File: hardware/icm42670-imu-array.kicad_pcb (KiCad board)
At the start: 4 copper layers, 40 x 40 mm, 63 parts, among them J1 TC2030-NL, J2 USB_B_Micro, J3 Conn_02x10_Odd_Even, SW1 PTS810, U1 ICM-42670-P, U10 MCP73812T-420I-OT, U2 ICM-42670-P, U3 ICM-42670-P, U4 ICM-42670-P, U5 ICM-42670-P, U6 ICM-42670-P, U7 ICM-42670-P, U8 ICM-42670-P, U9 MDBT50Q-P1MV2

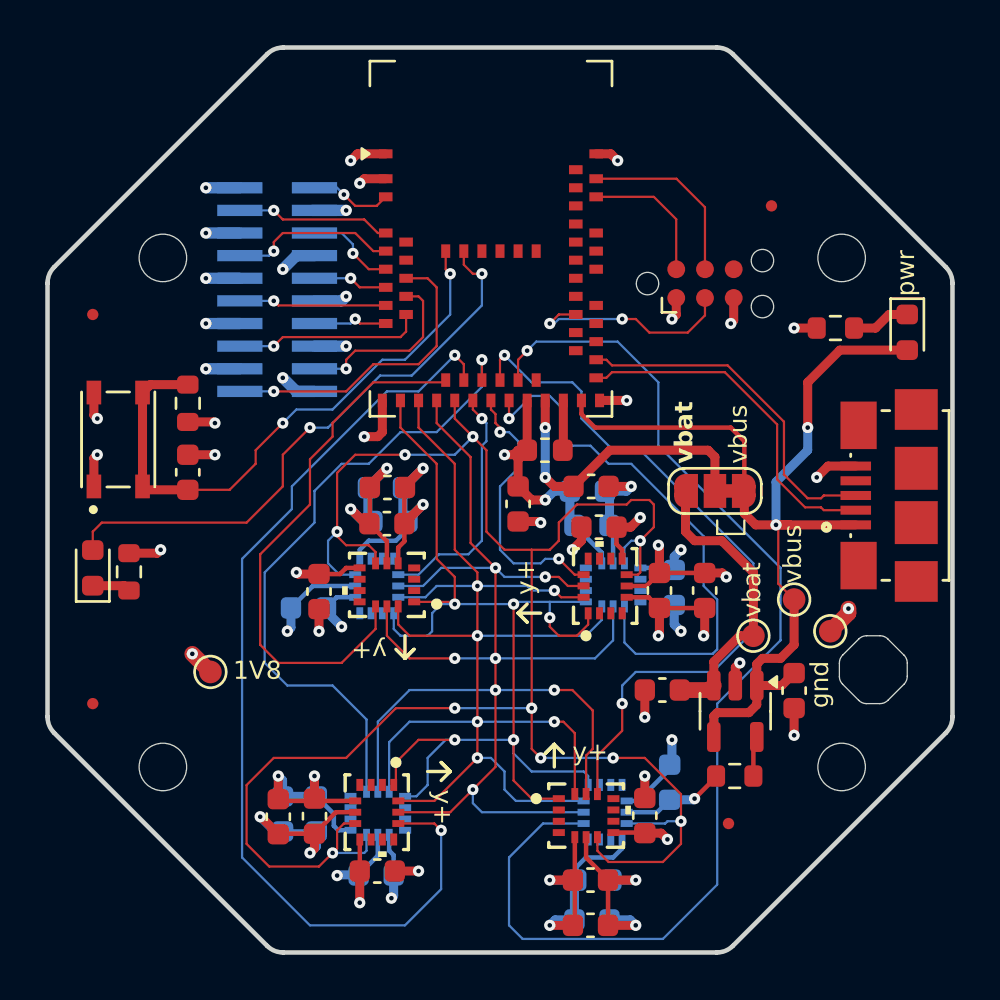
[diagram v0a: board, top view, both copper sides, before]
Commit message: feat: add round tracks
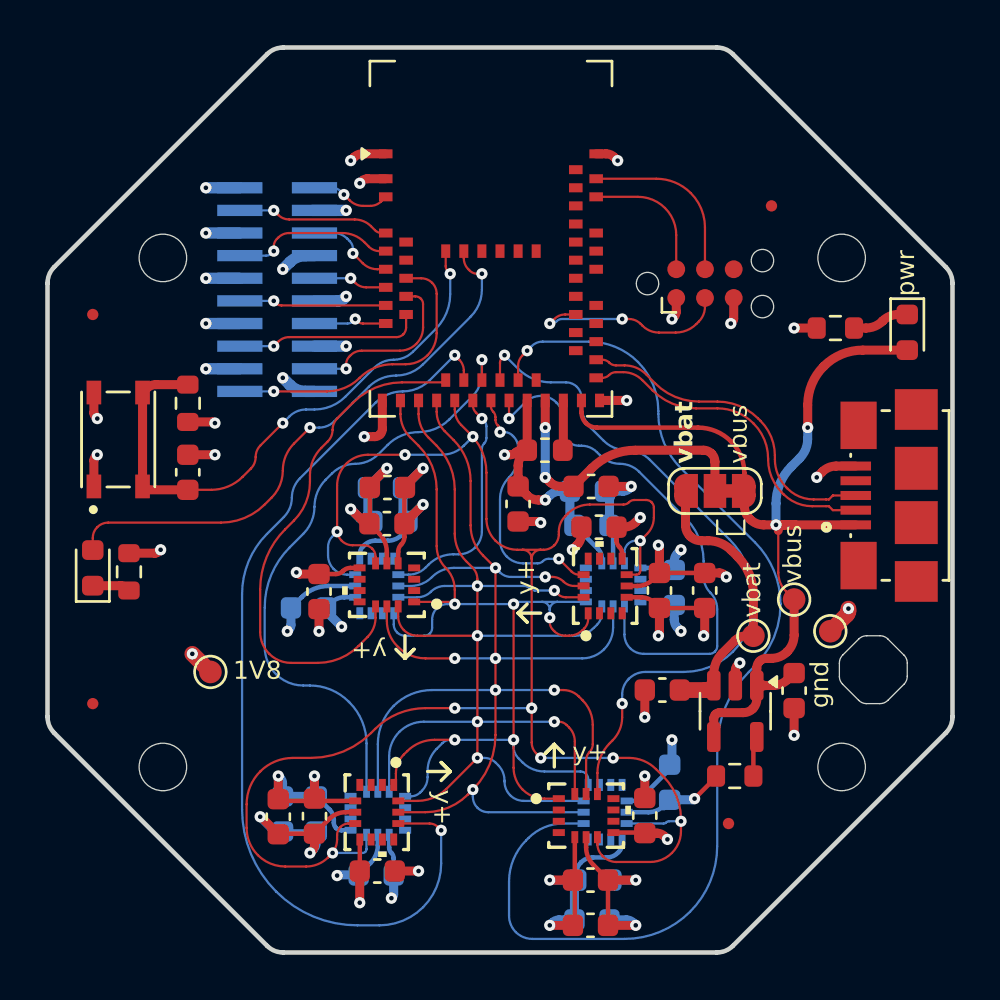
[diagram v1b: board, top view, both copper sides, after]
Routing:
- net CS5: track 51.1 -> 49.3 mm
- net FSYNC: track 86.9 -> 85.4 mm
- net GND: track 95.6 -> 94.1 mm
- net SCLK: track 67.7 -> 66.2 mm
- net +1V8: track 81.6 -> 80.2 mm
- net CS3: track 43.5 -> 42.2 mm
- net CS6: track 28.6 -> 27.5 mm
- net CS1: track 31.7 -> 30.6 mm
- net SDI: track 60.2 -> 59.1 mm
- net USB_DN: track 15.5 -> 14.5 mm
- net CS4: track 24.0 -> 23.0 mm
- net USB_DP: track 15.4 -> 14.5 mm
- net CS7: track 24.3 -> 23.6 mm
- net USR_LED: track 25.9 -> 25.2 mm
- net Net-(U9-P1.04): track 26.4 -> 25.8 mm
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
